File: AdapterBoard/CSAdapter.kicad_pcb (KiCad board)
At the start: 2 copper layers, 10.4 x 18 mm, 3 parts, among them J1 Conn_01x04, J2 Conn_01x06, SW1 CHS-01

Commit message: Design rules and gerber files
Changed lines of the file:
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@@
 	)
 	(setup
+		(stackup
+			(layer "F.SilkS"
+				(type "Top Silk Screen")
+			)
+			(layer "F.Paste"
+				(type "Top Solder Paste")
+			)
+			(layer "F.Mask"
+				(type "Top Solder Mask")
+				(thickness 0.01)
+			)
+			(layer "F.Cu"
+				(type "copper")
+				(thickness 0.035)
+			)
+			(layer "dielectric 1"
+				(type "core")
+				(thickness 1.51)
+				(material "FR4")
+				(epsilon_r 4.5)
+				(loss_tangent 0.02)
+			)
+			(layer "B.Cu"
+				(type "copper")
+				(thickness 0.035)
+			)
+			(layer "B.Mask"
+				(type "Bottom Solder Mask")
+				(thickness 0.01)
+			)
+			(layer "B.Paste"
+				(type "Bottom Solder Paste")
+			)
+			(layer "B.SilkS"
+				(type "Bottom Silk Screen")
+			)
+			(copper_finish "None")
+			(dielectric_constraints no)
+		)
 		(pad_to_mask_clearance 0)
 		(allow_soldermask_bridges_in_footprints no)
@@
 			(plot_on_all_layers_selection 0x0000000_00000000)
 			(disableapertmacros no)
-			(usegerberextensions no)
+			(usegerberextensions yes)
 			(usegerberattributes yes)
 			(usegerberadvancedattributes yes)
-			(creategerberjobfile yes)
+			(creategerberjobfile no)
 			(dashed_line_dash_ratio 12.000000)
 			(dashed_line_gap_ratio 3.000000)
@@
 			(psa4output no)
 			(plotreference yes)
-			(plotvalue yes)
+			(plotvalue no)
 			(plotfptext yes)
 			(plotinvisibletext no)
 			(sketchpadsonfab no)
-			(subtractmaskfromsilk no)
+			(subtractmaskfromsilk yes)
 			(outputformat 1)
 			(mirror no)
-			(drillshape 1)
+			(drillshape 0)
 			(scaleselection 1)
-			(outputdirectory "")
+			(outputdirectory "Gerber/")
 		)
 	)
@@
 				(font
 					(size 1 1)
-					(thickness 0.15)
+					(thickness 0.2)
+					(bold yes)
 				)
 			)
@@
 				(font
 					(size 1 1)
-					(thickness 0.15)
-				)
-			)
+					(thickness 0.2)
+					(bold yes)
+				)
+			)

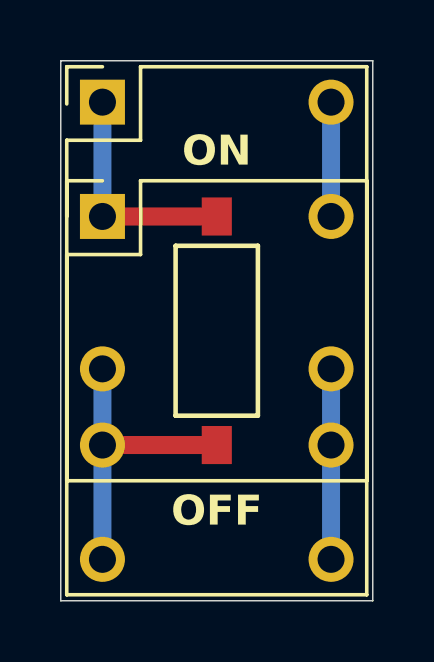
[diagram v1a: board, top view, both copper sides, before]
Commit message: Fix adapter board for dual layer
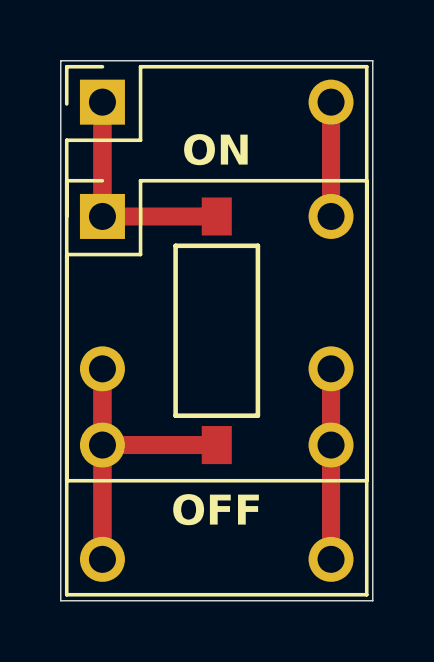
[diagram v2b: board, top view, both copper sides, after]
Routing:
- net Net-(J1-Pin_3): track 6.35 -> 12.7 mm
- net Net-(J1-Pin_2): track 10.2 -> 16.5 mm
- net Net-(J1-Pin_4): track 3.81 -> 7.62 mm
- net Net-(J1-Pin_1): track 7.62 -> 11.4 mm
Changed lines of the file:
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@@
+	(segment
+		(start 101.39 112.81)
+		(end 101.39 116.62)
+		(width 0.6)
+		(layer "F.Cu")
+		(net 1)
+	)
 	(segment
 		(start 101.39 112.81)
 		(end 105.2 112.81)
+		(width 0.6)
+		(layer "F.Cu")
+		(net 1)
+	)
+	(segment
+		(start 101.39 110.27)
+		(end 101.39 112.81)
 		(width 0.6)
 		(layer "F.Cu")
@@
 	)
 	(segment
+		(start 109.01 110.27)
+		(end 109.01 112.81)
+		(width 0.6)
+		(layer "F.Cu")
+		(net 2)
+	)
+	(segment
+		(start 109.01 112.81)
+		(end 109.01 116.62)
+		(width 0.6)
+		(layer "F.Cu")
+		(net 2)
+	)
+	(segment
 		(start 109.01 116.62)
 		(end 109.01 112.81)
@@
 		(layer "B.Cu")
 		(net 2)
+	)
+	(segment
+		(start 101.39 101.38)
+		(end 101.39 105.19)
+		(width 0.6)
+		(layer "F.Cu")
+		(net 3)
 	)
 	(segment
@@
 	)
 	(segment
+		(start 109.01 101.38)
+		(end 109.01 105.19)
+		(width 0.6)
+		(layer "F.Cu")
+		(net 4)
+	)
+	(segment
